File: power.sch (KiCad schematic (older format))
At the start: 44 parts

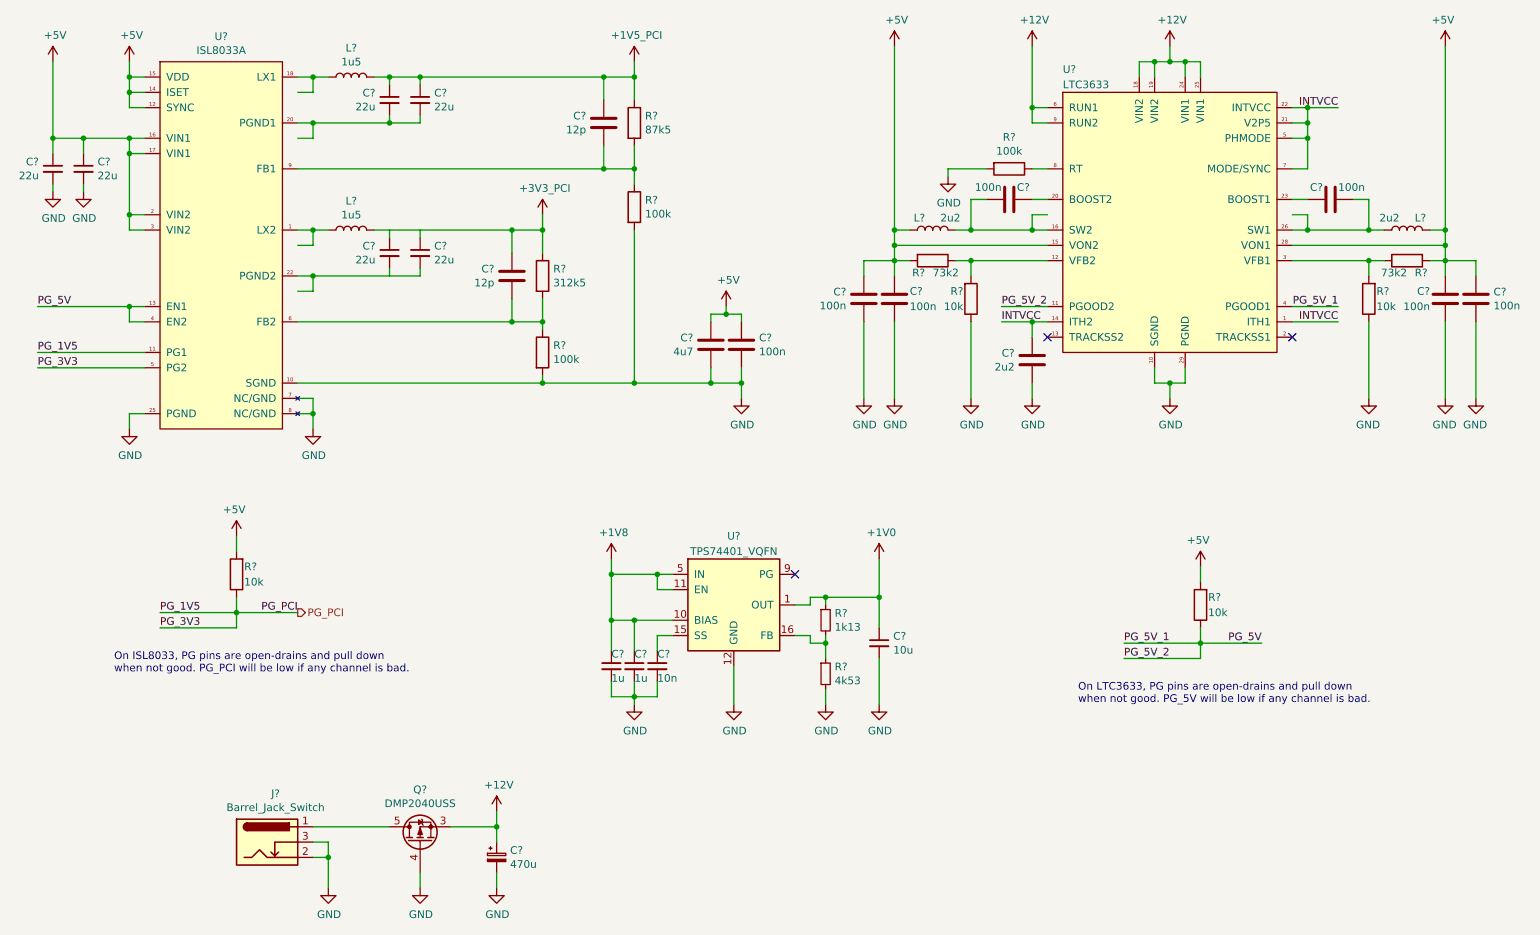
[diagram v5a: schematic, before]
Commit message: sch: Make ERC happy with dummy power outputs
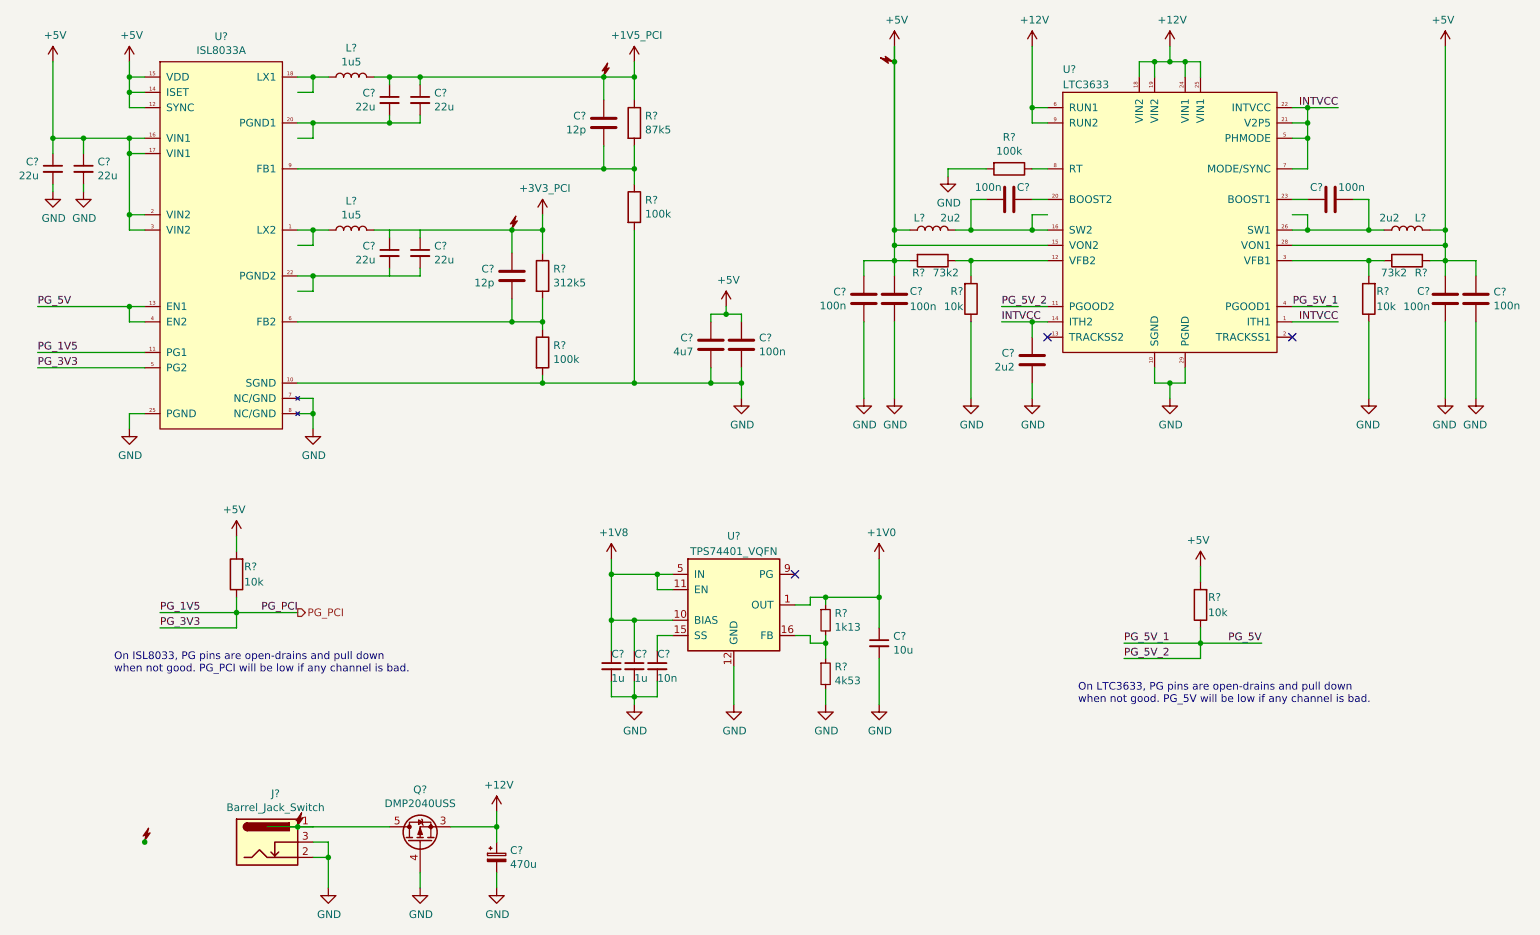
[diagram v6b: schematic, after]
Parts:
- added DS? (x5): DummySupply, symbol pimouss-motherboard:DummySupply
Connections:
- wire segments 230 -> 234
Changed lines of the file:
@@
 Wire Wire Line
 	4500 3800 5100 3800
+$Comp
+L pimouss-motherboard:DummySupply DS?
+U 1 1 5DE84E2B
+P 2900 6700
+AR Path="/5DE84E2B" Ref="DS?"  Part="1"
+AR Path="/5D0C4621/5DE84E2B" Ref="DS?"  Part="1"
+F 0 "DS?" H 2900 6700 50  0001 C CNN
+F 1 "DummySupply" H 2900 6700 50  0001 C CNN
+F 2 "" H 2900 6700 50  0001 C CNN
+F 3 "" H 2900 6700 50  0001 C CNN
+	1    2900 6700
+	1    0    0    -1
+$EndComp
+$Comp
+L pimouss-motherboard:DummySupply DS?
+U 1 1 5DEDED3F
+P 4900 1800
+AR Path="/5DEDED3F" Ref="DS?"  Part="1"
+AR Path="/5D0C4621/5DEDED3F" Ref="DS?"  Part="1"
+F 0 "DS?" H 4900 1800 50  0001 C CNN
+F 1 "DummySupply" H 4900 1800 50  0001 C CNN
+F 2 "" H 4900 1800 50  0001 C CNN
+F 3 "" H 4900 1800 50  0001 C CNN
+	1    4900 1800
+	1    0    0    -1
+$EndComp
+$Comp
+L pimouss-motherboard:DummySupply DS?
+U 1 1 5DEEC95C
+P 4300 2800
+AR Path="/5DEEC95C" Ref="DS?"  Part="1"
+AR Path="/5D0C4621/5DEEC95C" Ref="DS?"  Part="1"
+F 0 "DS?" H 4300 2800 50  0001 C CNN
+F 1 "DummySupply" H 4300 2800 50  0001 C CNN
+F 2 "" H 4300 2800 50  0001 C CNN
+F 3 "" H 4300 2800 50  0001 C CNN
+	1    4300 2800
+	1    0    0    -1
+$EndComp
+$Comp
+L pimouss-motherboard:DummySupply DS?
+U 1 1 5DEFA4BC
+P 6800 1700
+AR Path="/5DEFA4BC" Ref="DS?"  Part="1"
+AR Path="/5D0C4621/5DEFA4BC" Ref="DS?"  Part="1"
+F 0 "DS?" H 6800 1700 50  0001 C CNN
+F 1 "DummySupply" H 6800 1700 50  0001 C CNN
+F 2 "" H 6800 1700 50  0001 C CNN
+F 3 "" H 6800 1700 50  0001 C CNN
+	1    6800 1700
+	0    -1   -1   0
+$EndComp
+$Comp
+L pimouss-motherboard:DummySupply DS?
+U 1 1 5DF17E48
+P 1900 6800
+AR Path="/5DF17E48" Ref="DS?"  Part="1"
+AR Path="/5D0C4621/5DF17E48" Ref="DS?"  Part="1"
+F 0 "DS?" H 1900 6800 50  0001 C CNN
+F 1 "DummySupply" H 1900 6800 50  0001 C CNN
+F 2 "" H 1900 6800 50  0001 C CNN
+F 3 "" H 1900 6800 50  0001 C CNN
+	1    1900 6800
+	1    0    0    -1
+$EndComp
+Connection ~ 2900 6700
+Wire Wire Line
+	2900 6700 3000 6700
+Wire Wire Line
+	2700 6700 2900 6700
+Connection ~ 1900 6800
+Wire Wire Line
+	6800 1600 6800 1700
+Connection ~ 6800 1700
+Wire Wire Line
+	6800 1700 6800 2800
 $EndSCHEMATC

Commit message: lib, sch: Misc changes to make ERC happy
- add resistors to PCIe switch GPIOs
- add NC flags on PHY unused LED outputs
- add dummy supply on Earth PSU
- add dummy supply on PHY ref clock's VCC
- LTC3633: deduplicate SW1/2 outputs
- ILS8033: deduplicate LX1/2 and PGND1/2 outputs
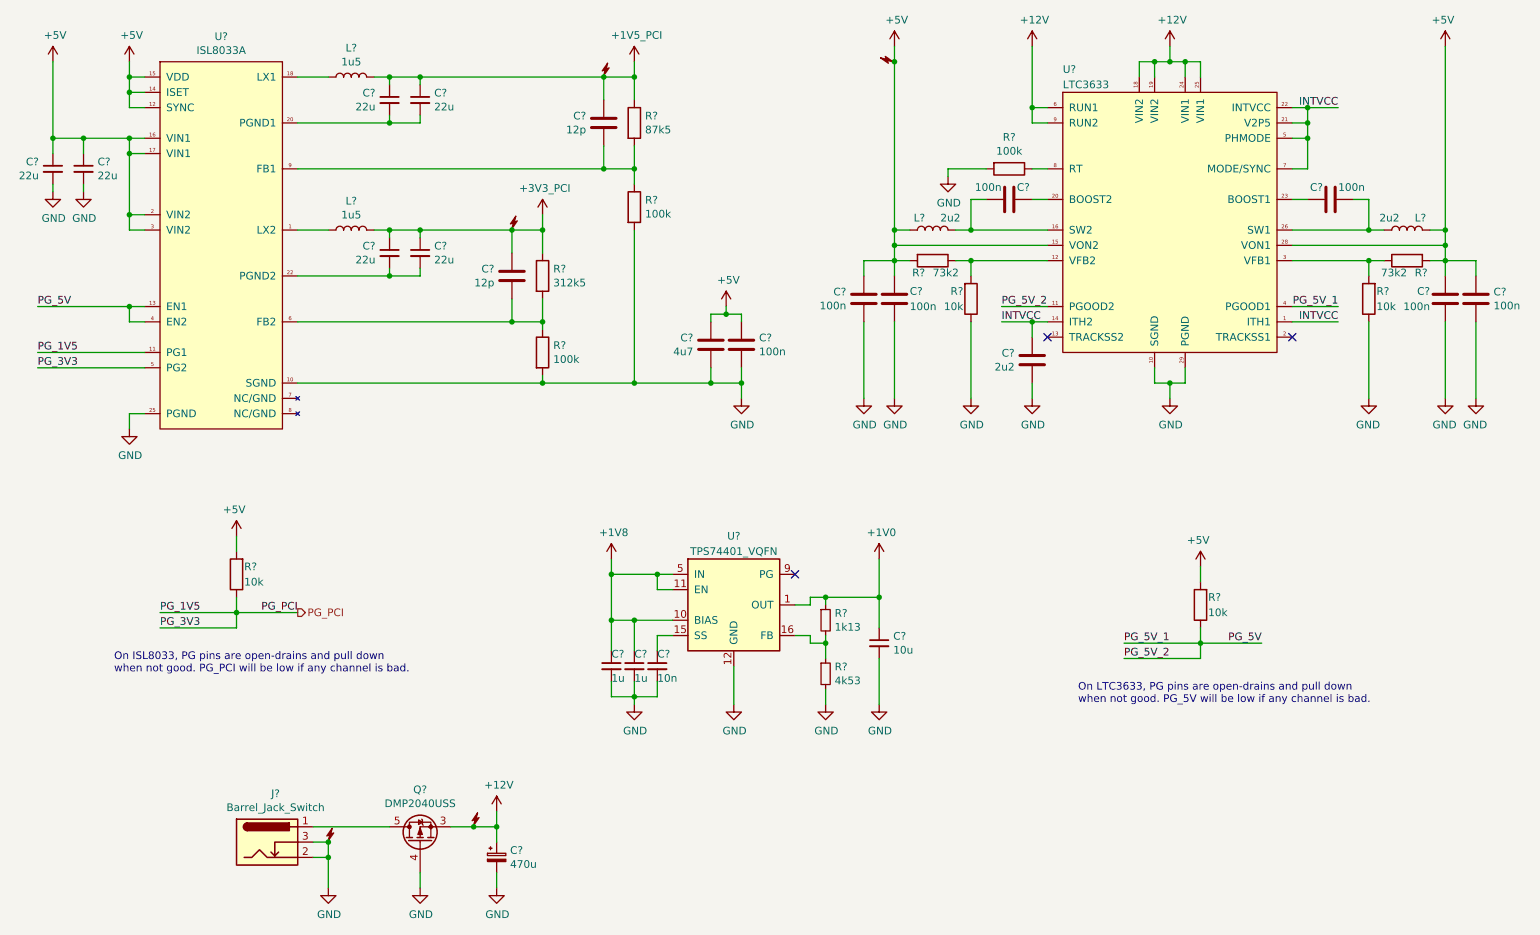
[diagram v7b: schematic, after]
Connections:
- wire segments 234 -> 213
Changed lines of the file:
@@
 $EndComp
-Wire Wire Line
-	2900 1800 3000 1800
-Wire Wire Line
-	2900 1900 3000 1900
-Wire Wire Line
-	3000 1900 3000 1800
-Connection ~ 3000 1800
-Wire Wire Line
-	3000 1800 3100 1800
-Wire Wire Line
-	2900 2100 3000 2100
-Wire Wire Line
-	3000 2100 3000 2200
-Wire Wire Line
-	3000 2200 2900 2200
 Wire Wire Line
 	5100 1800 5100 1700
@@
 Wire Wire Line
 	4900 2400 5100 2400
-Connection ~ 3000 2100
 Wire Wire Line
 	2900 2400 4900 2400
@@
 $EndComp
 Wire Wire Line
-	2900 2800 3000 2800
-Wire Wire Line
-	2900 2900 3000 2900
-Wire Wire Line
-	3000 2900 3000 2800
-Connection ~ 3000 2800
-Wire Wire Line
-	3000 2800 3100 2800
-Wire Wire Line
-	2900 3100 3000 3100
-Wire Wire Line
-	3000 3100 3000 3200
-Wire Wire Line
-	3000 3200 2900 3200
-Wire Wire Line
 	4500 2800 4500 2700
 $Comp
@@
 Wire Wire Line
 	4300 3400 4500 3400
-Connection ~ 3000 3100
 Wire Wire Line
 	2900 3400 4300 3400
@@
 Wire Wire Line
 	5700 3350 5800 3350
-Wire Wire Line
-	2900 3900 3000 3900
-Wire Wire Line
-	3000 3900 3000 4000
-Wire Wire Line
-	2900 4000 3000 4000
-Connection ~ 3000 4000
-Wire Wire Line
-	3000 4000 3000 4100
-$Comp
-L power:GND #PWR?
-U 1 1 5D10C724
-P 3000 4100
-F 0 "#PWR?" H 3000 3850 50  0001 C CNN
-F 1 "GND" H 3005 3927 50  0000 C CNN
-F 2 "" H 3000 4100 50  0001 C CNN
-F 3 "" H 3000 4100 50  0001 C CNN
-	1    3000 4100
-	1    0    0    -1
-$EndComp
 $Comp
 L pimouss-motherboard:LTC3633 U?
@@
 	7700 2600 7800 2600
 Wire Wire Line
-	7800 2700 7700 2700
-Wire Wire Line
-	7700 2700 7700 2800
-Wire Wire Line
-	7700 2800 7800 2800
-Wire Wire Line
-	7700 2800 7300 2800
-Wire Wire Line
 	7300 2800 7300 2600
 Wire Wire Line
 	7300 2600 7400 2600
-Connection ~ 7700 2800
 $Comp
 L Device:L L?
@@
 	7700 1600 7700 2000
 Wire Wire Line
-	6800 1600 6800 2800
+	6800 1600 6800 1700
 $Comp
 L power:+5V #PWR?
@@
 	9500 2600 9400 2600
 Wire Wire Line
-	9400 2700 9500 2700
-Wire Wire Line
-	9500 2700 9500 2800
-Wire Wire Line
-	9500 2800 9400 2800
-Wire Wire Line
-	9500 2800 9900 2800
-Wire Wire Line
 	9900 2800 9900 2600
 Wire Wire Line
 	9900 2600 9800 2600
-Connection ~ 9500 2800
 $Comp
 L Device:L L?
@@
 	0    -1   -1   0
 $EndComp
-Wire Wire Line
-	3000 6700 3500 6700
 $Comp
 L power:GND #PWR?
@@
 $EndComp
 Wire Wire Line
-	3900 6700 4200 6700
-Wire Wire Line
 	4200 6700 4200 6600
 Wire Wire Line
@@
 	1    0    0    -1
 $EndComp
-Wire Wire Line
-	3000 2100 3500 2100
 $Comp
 L Device:C_Small C?
@@
 	3700 2050 3700 2100
 Wire Wire Line
-	3000 3100 3700 3100
-Wire Wire Line
-	3400 2800 4300 2800
+	3400 2800 3500 2800
 $Comp
 L Device:C_Small C?
@@
 Wire Wire Line
 	4500 3800 5100 3800
-$Comp
-L pimouss-motherboard:DummySupply DS?
-U 1 1 5DE84E2B
-P 2900 6700
-AR Path="/5DE84E2B" Ref="DS?"  Part="1"
-AR Path="/5D0C4621/5DE84E2B" Ref="DS?"  Part="1"
-F 0 "DS?" H 2900 6700 50  0001 C CNN
-F 1 "DummySupply" H 2900 6700 50  0001 C CNN
-F 2 "" H 2900 6700 50  0001 C CNN
-F 3 "" H 2900 6700 50  0001 C CNN
-	1    2900 6700
-	1    0    0    -1
-$EndComp
 $Comp
 L pimouss-motherboard:DummySupply DS?
@@
 L pimouss-motherboard:DummySupply DS?
 U 1 1 5DF17E48
-P 1900 6800
+P 3100 6800
 AR Path="/5DF17E48" Ref="DS?"  Part="1"
 AR Path="/5D0C4621/5DF17E48" Ref="DS?"  Part="1"
-F 0 "DS?" H 1900 6800 50  0001 C CNN
-F 1 "DummySupply" H 1900 6800 50  0001 C CNN
-F 2 "" H 1900 6800 50  0001 C CNN
-F 3 "" H 1900 6800 50  0001 C CNN
-	1    1900 6800
-	1    0    0    -1
-$EndComp
-Connection ~ 2900 6700
-Wire Wire Line
-	2900 6700 3000 6700
-Wire Wire Line
-	2700 6700 2900 6700
-Connection ~ 1900 6800
-Wire Wire Line
-	6800 1600 6800 1700
+F 0 "DS?" H 3100 6800 50  0001 C CNN
+F 1 "DummySupply" H 3100 6800 50  0001 C CNN
+F 2 "" H 3100 6800 50  0001 C CNN
+F 3 "" H 3100 6800 50  0001 C CNN
+	1    3100 6800
+	1    0    0    -1
+$EndComp
 Connection ~ 6800 1700
 Wire Wire Line
 	6800 1700 6800 2800
+Wire Wire Line
+	2900 1800 3100 1800
+Wire Wire Line
+	2900 2100 3500 2100
+Wire Wire Line
+	2900 2800 3100 2800
+Wire Wire Line
+	2900 3100 3500 3100
+Connection ~ 3500 3100
+Wire Wire Line
+	3500 3100 3700 3100
+Connection ~ 3500 2800
+Wire Wire Line
+	3500 2800 3700 2800
+Connection ~ 3700 2800
+Wire Wire Line
+	3700 2800 4300 2800
+Wire Wire Line
+	9400 2800 9900 2800
+Wire Wire Line
+	7300 2800 7800 2800
+Wire Wire Line
+	3900 6700 4050 6700
+$Comp
+L pimouss-motherboard:DummySupply DS?
+U 1 1 5DE84E2B
+P 4050 6700
+AR Path="/5DE84E2B" Ref="DS?"  Part="1"
+AR Path="/5D0C4621/5DE84E2B" Ref="DS?"  Part="1"
+F 0 "DS?" H 4050 6700 50  0001 C CNN
+F 1 "DummySupply" H 4050 6700 50  0001 C CNN
+F 2 "" H 4050 6700 50  0001 C CNN
+F 3 "" H 4050 6700 50  0001 C CNN
+	1    4050 6700
+	1    0    0    -1
+$EndComp
+Connection ~ 4050 6700
+Wire Wire Line
+	4050 6700 4200 6700
+Wire Wire Line
+	3000 6700 3500 6700
+Connection ~ 3100 6800
 $EndSCHEMATC

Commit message: sch: Annotate & associate symbols with footprints
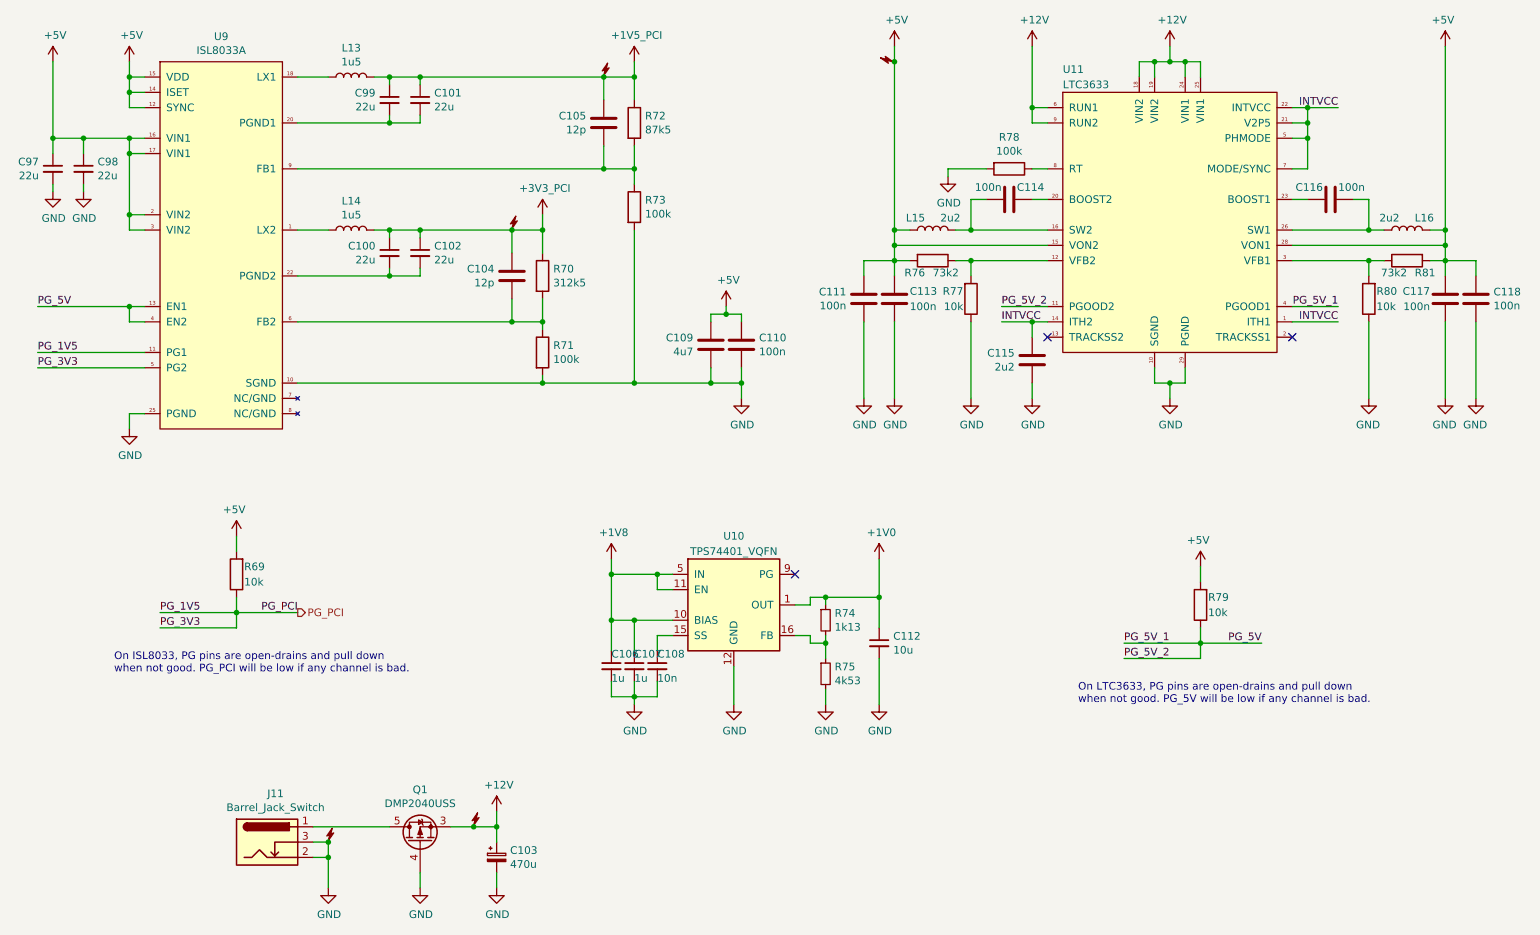
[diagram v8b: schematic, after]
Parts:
- removed DS? (x5): DummySupply, symbol pimouss-motherboard:DummySupply
- C100, C101, C102, C97, C98, C99: renamed from C?; footprint (none) -> Capacitor_SMD:C_0805_2012Metric
- C103: renamed from C?; footprint (none) -> Capacitor_SMD:CP_Elec_10x10
- C104, C105, C106, C107, C108, C109, C110, C111, C112, C113, C114, C115, C116, C117, C118: renamed from C?; footprint (none) -> Capacitor_SMD:C_0603_1608Metric
- J11: renamed from J?; footprint (none) -> Connector_BarrelJack:BarrelJack_Horizontal
- L13, L14, L15, L16: renamed from L?; footprint (none) -> pimouss-motherboard:L_Vishay_IHHP-0806
- R69, R70, R71, R72, R73, R74, R75, R76, R77, R78, R79, R80, R81: renamed from R?; footprint (none) -> Resistor_SMD:R_0603_1608Metric
- U10: renamed from U?; footprint (none) -> Package_DFN_QFN:Texas_S-PVQFN-N20_EP3.15x3.15mm_ThermalVias
- gave numbers to parts that had none: 3
